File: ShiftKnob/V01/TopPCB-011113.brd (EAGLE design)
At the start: 32.6 x 32.6 mm, 6 parts, among them IC1 74HC595D

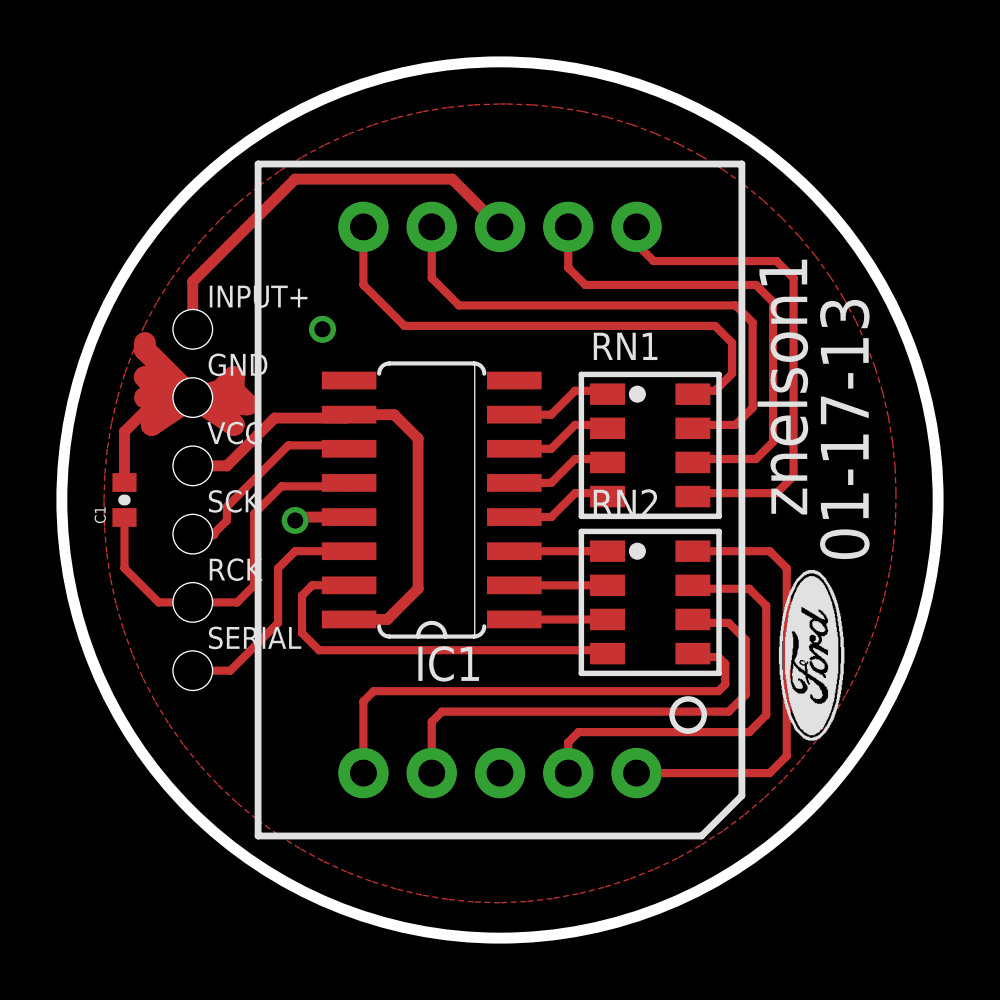
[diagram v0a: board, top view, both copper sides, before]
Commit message: all components added to BottomPCB schematic. added: MOSFETs, RGB LEDs x2, Motor connector, 7805 regulator
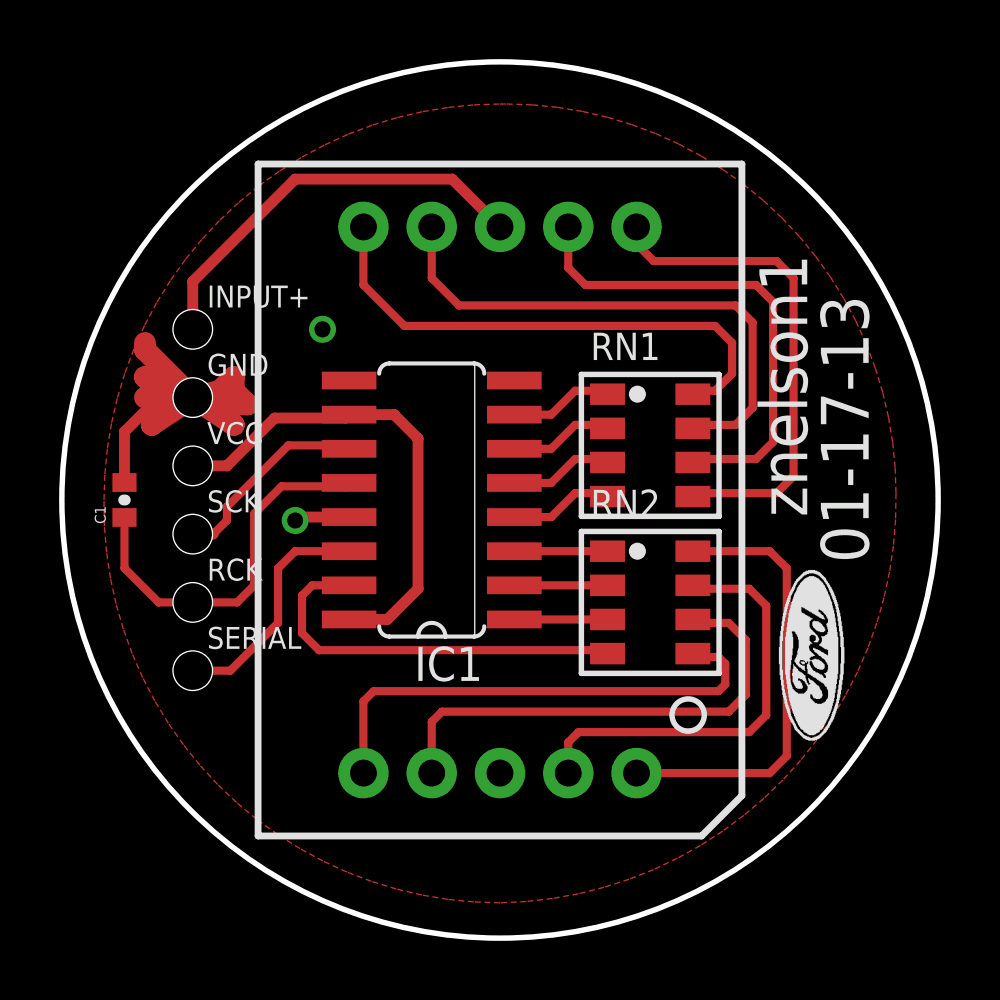
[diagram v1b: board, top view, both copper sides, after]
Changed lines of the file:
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@@
 <setting verticaltext="up"/>
 </settings>
-<grid distance="0.0254" unitdist="mm" unit="mm" style="lines" multiple="1" display="yes" altdistance="0.025" altunitdist="inch" altunit="inch"/>
+<grid distance="0.0254" unitdist="mm" unit="inch" style="lines" multiple="1" display="yes" altdistance="0.025" altunitdist="inch" altunit="inch"/>
 <layers>
 <layer number="1" name="Top" color="4" fill="1" visible="yes" active="yes"/>
@@
 <board>
 <plain>
-<circle x="17.78" y="17.78" radius="16.3" width="0.4064" layer="20"/>
+<circle x="17.78" y="17.78" radius="16.3" width="0.2032" layer="20"/>
 <text x="27.432" y="26.924" size="1.778" layer="21" rot="R270">znelson1</text>
 <text x="29.718" y="25.4" size="1.778" layer="21" rot="R270">01-17-13</text>

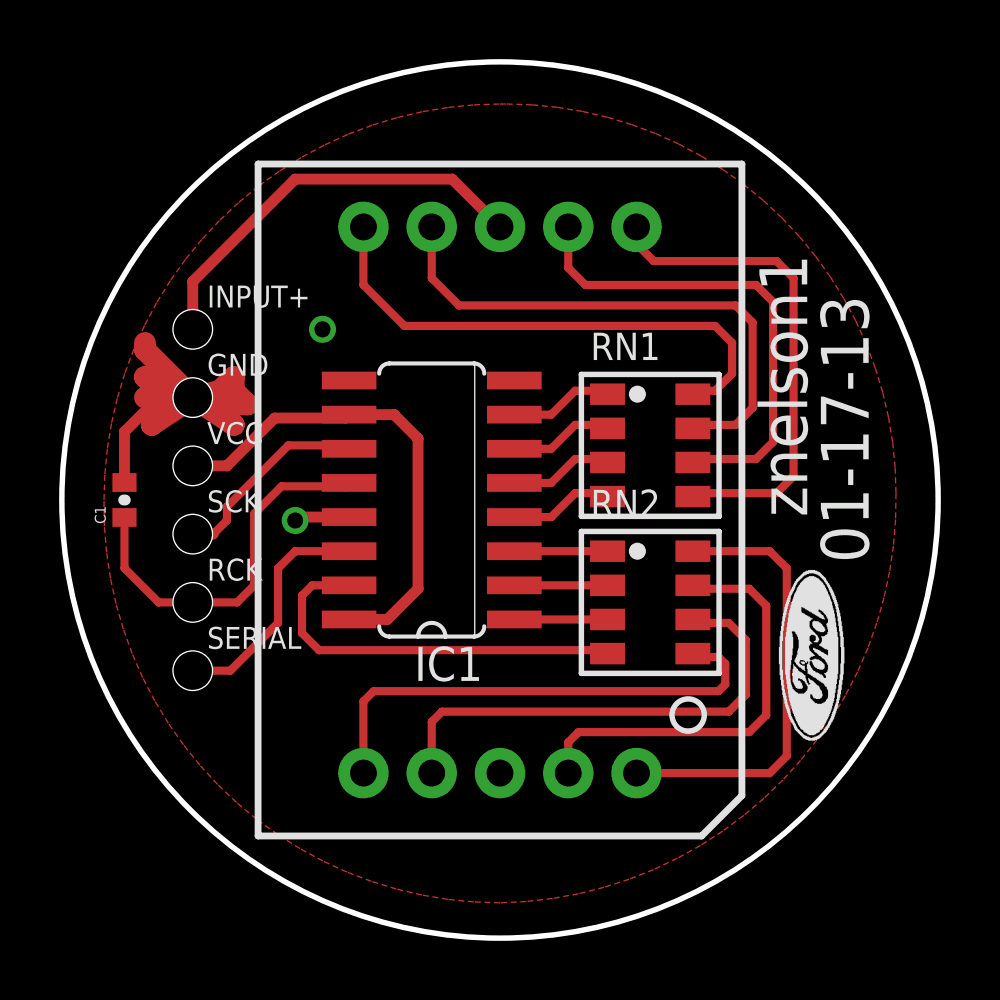
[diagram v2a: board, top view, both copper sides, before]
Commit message: add gnd trace on bottom layer. increase width of input+
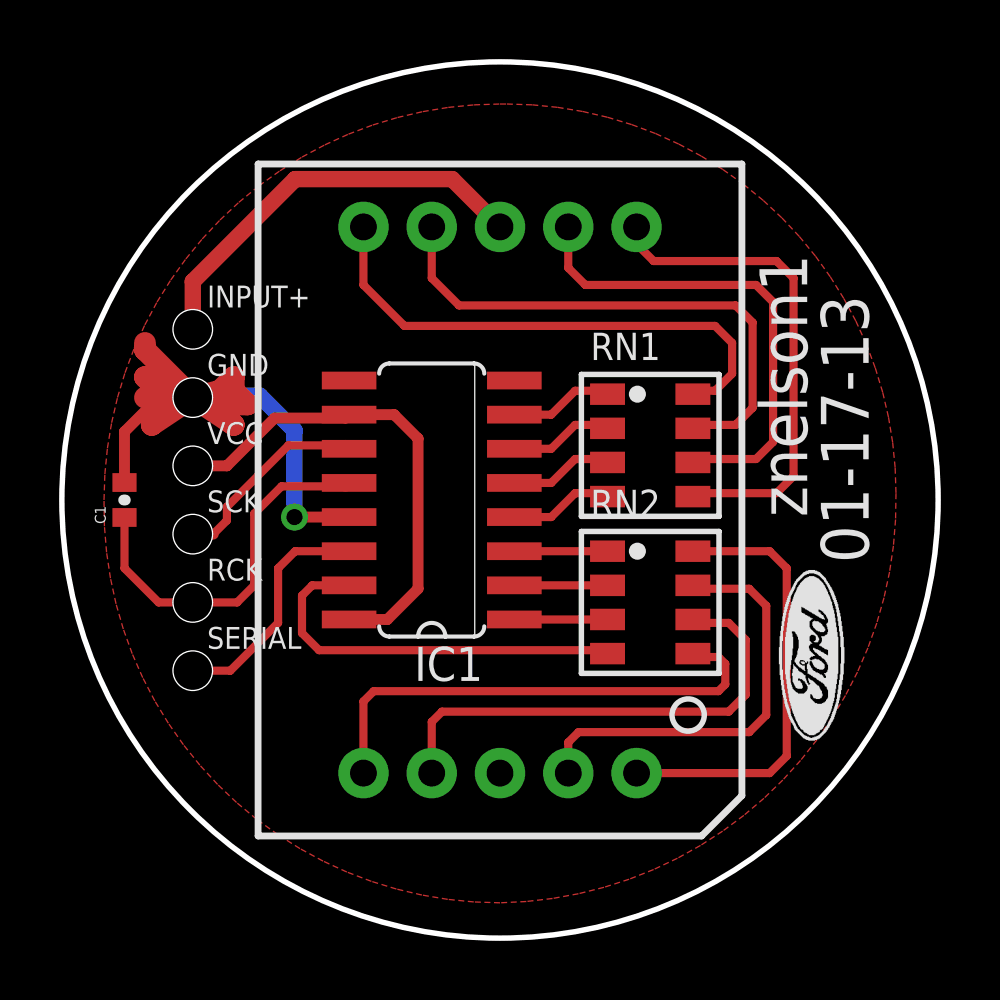
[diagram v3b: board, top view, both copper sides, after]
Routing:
- net GND: track 28.4 -> 36.0 mm
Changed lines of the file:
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@@
 </elements>
 <signals>
-<signal name="GND" airwireshidden="yes">
+<signal name="GND">
 <contactref element="IC1" pad="8"/>
 <contactref element="IC1" pad="13"/>
 <contactref element="C1" pad="2"/>
 <contactref element="JP1" pad="2"/>
-<wire x1="12.1666" y1="17.145" x2="10.287" y2="17.145" width="0.4064" layer="1"/>
-<wire x1="10.287" y1="17.145" x2="10.16" y2="17.018" width="0.4064" layer="1"/>
 <wire x1="6.35" y1="21.59" x2="5.08" y2="21.59" width="0.4064" layer="1"/>
 <wire x1="5.08" y1="21.59" x2="3.81" y2="20.32" width="0.4064" layer="1"/>
 <wire x1="3.81" y1="20.32" x2="3.81" y2="18.43" width="0.4064" layer="1"/>
-<polygon width="0.4064" layer="1" isolate="0.3048">
-<vertex x="3.048" y="17.78" curve="-90"/>
-<vertex x="17.78" y="32.512"/>
-<vertex x="18.034" y="32.512" curve="-90"/>
-<vertex x="32.512" y="18.034" curve="-90"/>
-<vertex x="17.78" y="2.794" curve="-90.979389"/>
-</polygon>
 <wire x1="4.572" y1="21.59" x2="6.35" y2="21.59" width="0.8128" layer="1"/>
 <wire x1="6.35" y1="21.59" x2="4.572" y2="22.352" width="0.8128" layer="1"/>
@@
 <wire x1="6.35" y1="21.59" x2="4.572" y2="23.368" width="0.8128" layer="1"/>
 <wire x1="4.572" y1="23.368" x2="4.572" y2="23.622" width="0.8128" layer="1"/>
-<via x="11.176" y="24.13" extent="1-16" drill="0.6"/>
-<wire x1="7.874" y1="20.574" x2="10.287" y2="17.145" width="0" layer="19" extent="1-1"/>
+<polygon width="0.4064" layer="1" isolate="0.3048">
+<vertex x="3.048" y="17.78" curve="-90"/>
+<vertex x="17.78" y="32.512"/>
+<vertex x="18.034" y="32.512" curve="-90"/>
+<vertex x="32.512" y="18.034" curve="-90"/>
+<vertex x="17.78" y="2.794" curve="-90.979389"/>
+</polygon>
+<wire x1="12.1666" y1="17.145" x2="10.1346" y2="17.145" width="0.4064" layer="1"/>
+<via x="10.1346" y="17.145" extent="1-16" drill="0.6"/>
+<wire x1="10.1346" y1="17.145" x2="10.1346" y2="20.3708" width="0.6096" layer="16"/>
+<wire x1="10.1346" y1="20.3708" x2="8.8392" y2="21.6662" width="0.6096" layer="16"/>
+<wire x1="8.8392" y1="21.6662" x2="6.4262" y2="21.6662" width="0.6096" layer="16"/>
+<wire x1="6.4262" y1="21.6662" x2="6.35" y2="21.59" width="0.4064" layer="16"/>
 </signal>
 <signal name="VCC">
@@
 <signal name="INPUT+">
 <contactref element="U$1" pad="8"/>
-<wire x1="16.002" y1="29.718" x2="17.78" y2="27.94" width="0.4064" layer="1"/>
+<wire x1="16.002" y1="29.718" x2="17.78" y2="27.94" width="0.6096" layer="1"/>
 <contactref element="JP1" pad="1"/>
-<wire x1="6.35" y1="24.13" x2="6.35" y2="25.908" width="0.4064" layer="1"/>
-<wire x1="10.16" y1="29.718" x2="6.35" y2="25.908" width="0.4064" layer="1"/>
-<wire x1="10.16" y1="29.718" x2="16.002" y2="29.718" width="0.4064" layer="1"/>
+<wire x1="6.35" y1="24.13" x2="6.35" y2="25.908" width="0.6096" layer="1"/>
+<wire x1="10.16" y1="29.718" x2="6.35" y2="25.908" width="0.6096" layer="1"/>
+<wire x1="10.16" y1="29.718" x2="16.002" y2="29.718" width="0.6096" layer="1"/>
 </signal>
 <signal name="SCK">
@@
 <wire x1="25.2095" y1="13.208" x2="24.9555" y2="13.335" width="0.3048" layer="1"/>
 </signal>
-<signal name="N$6">
-<via x="10.16" y="17.018" extent="1-16" drill="0.6"/>
-</signal>
 <signal name="NC2">

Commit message: name components, add silk screen labels, copy name-date-logo to bottom layer, increase board diameter to 33mm
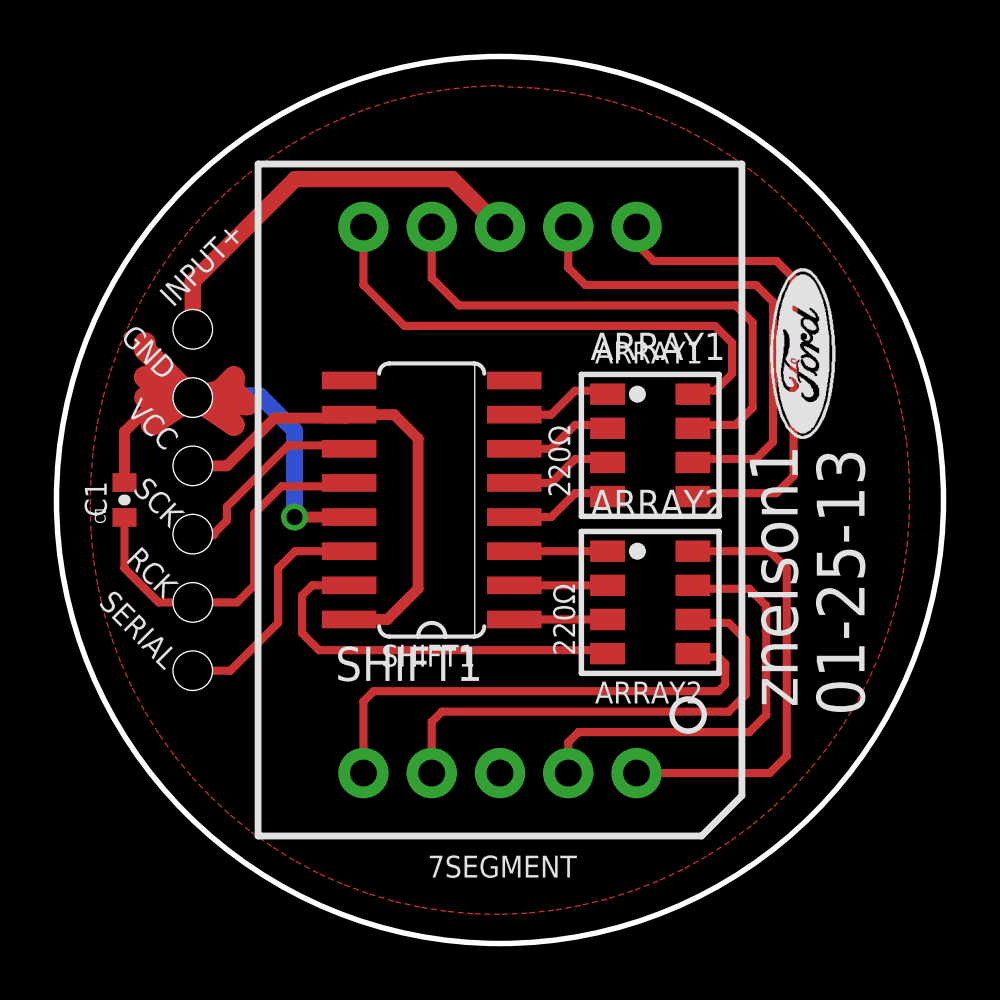
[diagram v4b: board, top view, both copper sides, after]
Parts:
- renumbered IC1 to SHIFT1, RN1 to ARRAY1, RN2 to ARRAY2, U$1 to 7SEGMENT
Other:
- board size 32.6 x 32.6 mm -> 33 x 33 mm
- board text added: "01-25-13"
- board text added: "220Ω"
- board text added: "7SEGMENT"
- board text added: "ARRAY1"
- board text added: "ARRAY2"
- board text added: "C1"
- board text added: "SHIFT1"
- board text removed: "01-17-13"
